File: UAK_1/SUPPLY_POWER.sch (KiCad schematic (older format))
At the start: 25 parts, among them X5 Крепежное_отверстие_d2, X6 Крепежное_отверстие_d2, X7 Крепежное_отверстие_d2

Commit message: 1B: заменены предохранители,обновлено питание,не добавлен второй дисплей
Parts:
- removed C11, C14: Конденсатор_керамический, N_RLC:Конденсатор_SMD_0603, symbol elements:Конденсатор_керамический
- removed DD2: Микросхема_DCDC_step_DOWN_MP2307DN, N_DD:SO-8_EP, symbol UAK_1-rescue:Микросхема_DCDC_step_DOWN_MP2307DN-elements_2020-UAK_0-rescue
- removed FU1: Предохранитель, N_RLC:Предохранитель_SMD_1812, symbol elements:Предохранитель
- removed G1: AC-DC-преобразователь_IRM-20-12, N_G:AC-DC_IRM-20-12, symbol UAK_1-rescue:AC-DC-преобразователь_IRM-20-12-elements_2020-UAK_0-rescue
- removed R18: Резистор_0,065Вт, N_RLC:Резистор_SMD_0603_0,065_Вт, symbol elements:Резистор_0,065Вт
- removed VD4, VD5: Диод_шоттки_SK16, N_VD_HL:Диод_SMB, symbol UAK_1-rescue:Диод_шоттки_SK16-elements_2020-UAK_0-rescue
- removed X5, X6, X7: Крепежное_отверстие_d2, MOTOR_ICO:Монтажное_отверстие_D2, symbol UAK_1-rescue:Крепежное_отверстие_d2-MOTOR_2020_components-UAK_0-rescue
- added DD2: Микросхема_DCDC_step_UP_LM2703, N_G:Преобразователь_LM2703_SOT-23-5, symbol elements:Микросхема_DCDC_step_UP_LM2703
- added G1: AC-DC-преобразователь_IRM-15-5, N_G:AC-DC_IRM-20-12, symbol elements_2020:AC-DC-преобразователь_IRM-15-5
- added VD2: Диод_шоттки_SK16, N_VD_HL:Диод_SMB, symbol UAK_1-rescue:Диод_шоттки_SK16-elements_2020-UAK_0-rescue
- C7: INFO 0,1мкФ/50В -> 10мкФ/25В; LINK https://www.chipdip.ru/product0/226236018 -> https://www.chipdip.ru/product/grm188r61e106m
- C8: INFO 10мкФ/25В -> 220пФ/50В; LINK https://www.chipdip.ru/product/grm188r61e106m -> https://www.chipdip.ru/product/grm188r71h392k
- C9: INFO 3900пФ/50В -> 10мкФ/25В; LINK https://www.chipdip.ru/product/grm188r71h392k -> https://www.chipdip.ru/product/grm188r61e106m
- L1: value Чип-индуктивность_10мкГн_1.8А_20проц. -> Чип-индуктивность_10мкГн_0.2А_20проц.; footprint N_RLC:Чип-индуктивность_SMD_SCD0503T -> N_RLC:Чип-индуктивность_SMD_0805; INFO 10мкГн/1,8А -> 10мкГн/0,2А; LINK https://www.chipdip.ru/product0/9000523874 -> https://www.chipdip.ru/product/mlz2012m100ht000-10
- R15: INFO 100 кОм -> 10 кОм
- R16: INFO 6,8 кОм -> 13,3 кОм
- R17: INFO 44,2 кОм -> 117 кОм
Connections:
- net labels added: 5V_NOISE
- net labels removed: 0V_RESERV, 12V_NOISE, 12V_OUT_G, 12V_RESERV, 5V_DC-DC, BOTTOM
- wire segments 85 -> 74
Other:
- note removed: "DC/DC 12V-5V + ОТВЕРСТИЯ ДЛЯ УСТАНОВКИ ПОКУПНОГО DC/DC НА СЛУЧАЙ НЕУДАЧИ"
- moved on the sheet: C10, C13, C16, L2

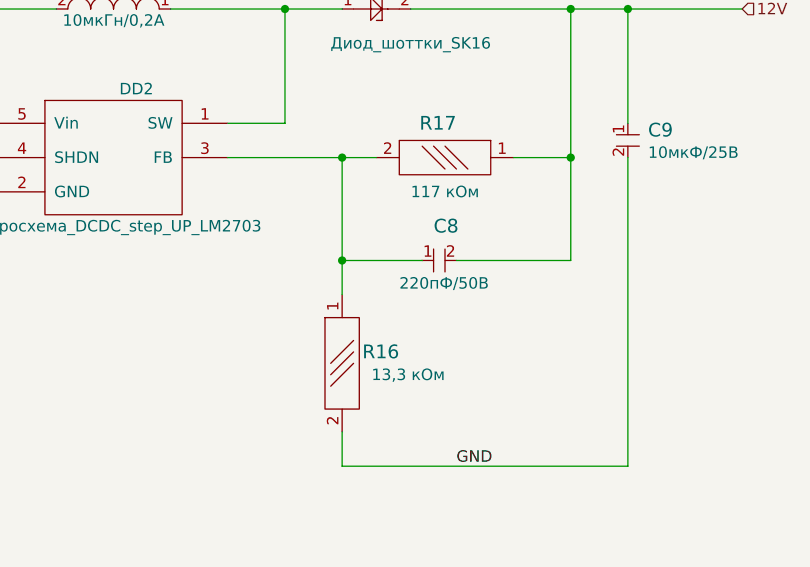
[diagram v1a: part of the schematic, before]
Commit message: обновлен перечень элементов
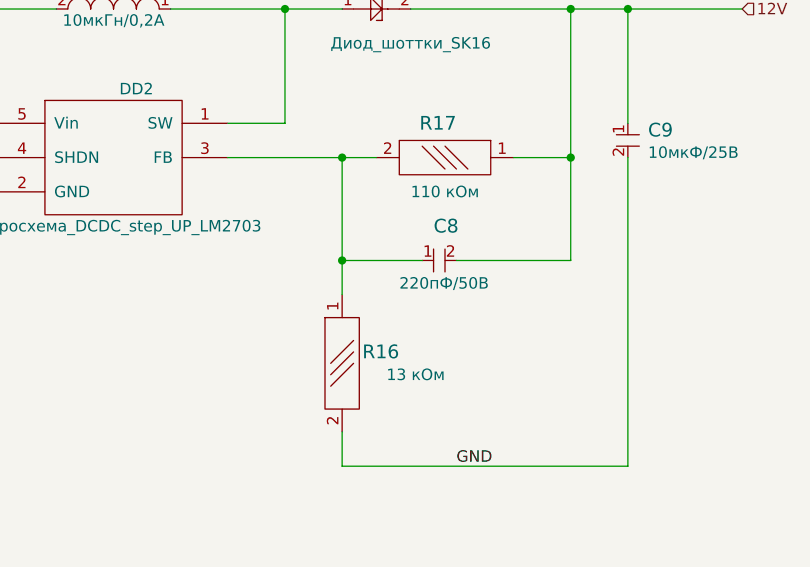
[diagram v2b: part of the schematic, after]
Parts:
- C10: Для заказа (none) -> Конденсатор 1210 0,022 мкФ 630В 10%
- C12, C13, C15, C16, C7, C9: LINK https://www.chipdip.ru/product/grm188r61e106m -> https://www.terraelectronica.ru/product/1489875; Для заказа (none) -> Конденсатор 0603 10 мкФ 25В 20%
- C8: LINK https://www.chipdip.ru/product/grm188r71h392k -> https://www.terraelectronica.ru/product/664080; Для заказа (none) -> Конденсатор 0603 220 пФ 50В 5%
- DD2: LINK (none) -> https://www.terraelectronica.ru/product/287900; Для заказа (none) -> DC-DC LM27313XMF/NOPB
- G1: Для заказа (none) -> AC-DC IRM-15-5
- G2: Для заказа (none) -> LDO LM1117GS-3.3
- L1: Для заказа (none) -> Чип-индуктивность 0805 10 мкГн 0,2А 20%
- L2: Для заказа (none) -> Дроссель B82731-T2132-A20
- R15: LINK (none) -> https://www.terraelectronica.ru/product/562124; Для заказа (none) -> Резистор 0603 10 кОм 5%
- R16: INFO 13,3 кОм -> 13 кОм; LINK (none) -> https://www.terraelectronica.ru/product/2782113; Для заказа (none) -> Резистор 0603 13 кОм 5%
- R17: INFO 117 кОм -> 110 кОм; Для заказа (none) -> Резистор 0603 110 кОм 5%
- VD2: LINK https://www.chipdip.ru/product/sk16-diotec -> https://www.terraelectronica.ru/product/129173; Для заказа (none) -> Диод шоттки SK16 (1А 60В)
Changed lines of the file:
@@
 F 4 "0,022мкФ/630В" V 3328 1788 50  0000 L CNN "INFO"
 F 5 "https://www.chipdip.ru/product/grm32qr72j223k" H 3250 1700 50  0001 C CNN "LINK"
+F 6 "Конденсатор 1210 0,022 мкФ 630В 10%" H 3250 1700 50  0001 C CNN "Для заказа"
 	1    3250 1700
 	0    1    1    0
@@
 F 3 "" H 6250 1650 60  0001 C CNN
 F 4 "10мкФ/25В" V 6328 1738 50  0000 L CNN "INFO"
-F 5 "https://www.chipdip.ru/product/grm188r61e106m" H 6250 1650 50  0001 C CNN "LINK"
+F 5 "https://www.terraelectronica.ru/product/1489875" H 6250 1650 50  0001 C CNN "LINK"
+F 6 "Конденсатор 0603 10 мкФ 25В 20%" H 6250 1650 50  0001 C CNN "Для заказа"
 	1    6250 1650
 	0    1    1    0
@@
 F 4 "https://www.chipdip.ru/product/b82731-t2132-a20" V 7250 1600 50  0001 C CNN "LINK"
 F 5 "2x6,8мГн/1,3А" V 7450 1650 50  0000 L CNN "INFO"
+F 6 "Дроссель B82731-T2132-A20" H 7250 1600 50  0001 C CNN "Для заказа"
 	1    7250 1600
 	0    1    1    0
@@
 F 3 "" H 8000 1650 60  0001 C CNN
 F 4 "10мкФ/25В" V 8078 1738 50  0000 L CNN "INFO"
-F 5 "https://www.chipdip.ru/product/grm188r61e106m" H 8000 1650 50  0001 C CNN "LINK"
+F 5 "https://www.terraelectronica.ru/product/1489875" H 8000 1650 50  0001 C CNN "LINK"
+F 6 "Конденсатор 0603 10 мкФ 25В 20%" H 8000 1650 50  0001 C CNN "Для заказа"
 	1    8000 1650
 	0    1    1    0
@@
 F 3 "https://static.chipdip.ru/lib/138/DOC004138838.pdf" H 4550 6000 50  0001 C CNN
 F 4 "https://www.chipdip.ru/product/lm1117gs-3.3" H 4550 6000 50  0001 C CNN "LINK"
+F 5 "LDO LM1117GS-3.3" H 4550 6000 50  0001 C CNN "Для заказа"
 	1    4550 6000
 	1    0    0    -1
@@
 F 3 "" H 4000 6150 60  0001 C CNN
 F 4 "10мкФ/25В" V 4078 6238 50  0000 L CNN "INFO"
-F 5 "https://www.chipdip.ru/product/grm188r61e106m" H 4000 6150 50  0001 C CNN "LINK"
+F 5 "https://www.terraelectronica.ru/product/1489875" H 4000 6150 50  0001 C CNN "LINK"
+F 6 "Конденсатор 0603 10 мкФ 25В 20%" H 4000 6150 50  0001 C CNN "Для заказа"
 	1    4000 6150
 	0    1    1    0
@@
 F 3 "" H 5500 6150 60  0001 C CNN
 F 4 "10мкФ/25В" V 5578 6238 50  0000 L CNN "INFO"
-F 5 "https://www.chipdip.ru/product/grm188r61e106m" H 5500 6150 50  0001 C CNN "LINK"
+F 5 "https://www.terraelectronica.ru/product/1489875" H 5500 6150 50  0001 C CNN "LINK"
+F 6 "Конденсатор 0603 10 мкФ 25В 20%" H 5500 6150 50  0001 C CNN "Для заказа"
 	1    5500 6150
 	0    1    1    0
@@
 F 4 "https://www.chipdip.ru/product/irm-15-5" H 4650 1100 50  0001 C CNN "LINK"
 F 5 "220В/5В" H 4650 1300 50  0000 C CNN "INFO"
+F 6 "AC-DC IRM-15-5" H 4300 1500 50  0001 C CNN "Для заказа"
 	1    4300 1500
 	1    0    0    -1
@@
 F 2 "N_G:Преобразователь_LM2703_SOT-23-5" H 5450 3500 50  0001 C CNN
 F 3 "" H 5450 3500 50  0001 C CNN
+F 4 "https://www.terraelectronica.ru/product/287900" H 5450 3500 50  0001 C CNN "LINK"
+F 5 "DC-DC LM27313XMF/NOPB" H 5450 3500 50  0001 C CNN "Для заказа"
 	1    5450 3500
 	1    0    0    -1
@@
 F 4 "10мкГн/0,2А" H 5350 2950 50  0000 C CNN "INFO"
 F 5 "https://www.chipdip.ru/product/mlz2012m100ht000-10" H 5400 2825 50  0001 C CNN "LINK"
+F 6 "Чип-индуктивность 0805 10 мкГн 0,2А 20%" H 5550 3000 50  0001 C CNN "Для заказа"
 	1    5550 3000
 	-1   0    0    -1
@@
 F 3 "https://static.chipdip.ru/lib/046/DOC003046730.pdf" H 6650 3000 50  0001 C CNN
 F 4 "1А, 60В" H 6925 2550 50  0001 C CNN "INFO"
-F 5 "https://www.chipdip.ru/product/sk16-diotec" H 6925 2675 50  0001 C CNN "LINK"
+F 5 "https://www.terraelectronica.ru/product/129173" H 6925 2675 50  0001 C CNN "LINK"
+F 6 "Диод шоттки SK16 (1А 60В)" H 6750 3000 50  0001 C CNN "Для заказа"
 	1    6750 3000
 	1    0    0    -1
@@
 F 3 "" H 4000 3550 60  0001 C CNN
 F 4 "10мкФ/25В" V 4078 3638 50  0000 L CNN "INFO"
-F 5 "https://www.chipdip.ru/product/grm188r61e106m" H 4000 3550 50  0001 C CNN "LINK"
+F 5 "https://www.terraelectronica.ru/product/1489875" H 4000 3550 50  0001 C CNN "LINK"
+F 6 "Конденсатор 0603 10 мкФ 25В 20%" H 4000 3550 50  0001 C CNN "Для заказа"
 	1    4000 3550
 	0    -1   1    0
@@
 F 3 "" H 8000 3550 60  0001 C CNN
 F 4 "10мкФ/25В" V 8078 3638 50  0000 L CNN "INFO"
-F 5 "https://www.chipdip.ru/product/grm188r61e106m" H 8000 3550 50  0001 C CNN "LINK"
+F 5 "https://www.terraelectronica.ru/product/1489875" H 8000 3550 50  0001 C CNN "LINK"
+F 6 "Конденсатор 0603 10 мкФ 25В 20%" H 8000 3550 50  0001 C CNN "Для заказа"
 	1    8000 3550
 	0    1    1    0
@@
 F 2 "N_RLC:Резистор_SMD_0603_0,065_Вт" H 7200 3650 60  0001 C CNN
 F 3 "" H 7200 3650 60  0001 C CNN
-F 4 "117 кОм" H 7050 3500 50  0000 L CNN "INFO"
+F 4 "110 кОм" H 7050 3500 50  0000 L CNN "INFO"
+F 5 "Резистор 0603 110 кОм 5%" H 7200 3650 50  0001 C CNN "Для заказа"
 	1    7200 3650
 	-1   0    0    -1
@@
 F 2 "N_RLC:Резистор_SMD_0603_0,065_Вт" H 6750 4550 60  0001 C CNN
 F 3 "" H 6750 4550 60  0001 C CNN
-F 4 "13,3 кОм" V 6800 4100 50  0000 L CNN "INFO"
+F 4 "13 кОм" V 6800 4100 50  0000 L CNN "INFO"
+F 5 "Резистор 0603 13 кОм 5%" H 6750 4550 50  0001 C CNN "Для заказа"
+F 6 "https://www.terraelectronica.ru/product/2782113" H 6750 4550 50  0001 C CNN "LINK"
 	1    6750 4550
 	0    -1   1    0
@@
 F 3 "" H 7150 4100 60  0001 C CNN
 F 4 "220пФ/50В" H 7000 4000 50  0000 L CNN "INFO"
-F 5 "https://www.chipdip.ru/product/grm188r71h392k" H 7150 4100 50  0001 C CNN "LINK"
+F 5 "https://www.terraelectronica.ru/product/664080" H 7150 4100 50  0001 C CNN "LINK"
+F 6 "Конденсатор 0603 220 пФ 50В 5%" H 7150 4100 50  0001 C CNN "Для заказа"
 	1    7150 4100
 	1    0    0    -1
@@
 F 3 "" H 4250 3550 60  0001 C CNN
 F 4 "10 кОм" V 4300 3150 50  0000 L CNN "INFO"
+F 5 "https://www.terraelectronica.ru/product/562124" H 4250 3550 50  0001 C CNN "LINK"
+F 6 "Резистор 0603 10 кОм 5%" H 4250 3550 50  0001 C CNN "Для заказа"
 	1    4250 3550
 	0    -1   1    0

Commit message: UAK.1C.M9, подготовлены gerber, схема, BOM
обновлена маркировка, заполнен BOM
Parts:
- G1: symbol elements_2020:AC-DC-преобразователь_IRM-15-5 -> UAK_1-rescue:AC-DC-преобразователь_IRM-15-5-elements_2020
- R16: INFO 13 кОм -> 10 кОм; LINK https://www.terraelectronica.ru/product/2782113 -> https://www.terraelectronica.ru/product/562124; Для заказа Резистор 0603 13 кОм 5% -> Резистор 0603 10 кОм 5%
- R17: INFO 110 кОм -> 82 кОм; LINK (none) -> https://www.terraelectronica.ru/product/2782214; Для заказа Резистор 0603 110 кОм 5% -> Резистор 0603 82 кОм 5%
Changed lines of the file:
@@
 EESchema Schematic File Version 4
 LIBS:UAK_1-cache
-EELAYER 30 0
+EELAYER 29 0
 EELAYER END
 $Descr A4 11693 8268
@@
 5V_NOISE
 $Comp
-L elements_2020:AC-DC-преобразователь_IRM-15-5 G1
+L UAK_1-rescue:AC-DC-преобразователь_IRM-15-5-elements_2020 G1
 U 1 1 5F6F4DEB
 P 4300 1500
+AR Path="/5F6F4DEB" Ref="G1"  Part="1"
+AR Path="/5F540B17/5F6F4DEB" Ref="G1"  Part="1"
 F 0 "G1" H 4850 1600 50  0000 C CNN
 F 1 "AC-DC-преобразователь_IRM-15-5" H 4650 1724 50  0001 C CNN
@@
 F 2 "N_RLC:Резистор_SMD_0603_0,065_Вт" H 7200 3650 60  0001 C CNN
 F 3 "" H 7200 3650 60  0001 C CNN
-F 4 "110 кОм" H 7050 3500 50  0000 L CNN "INFO"
-F 5 "Резистор 0603 110 кОм 5%" H 7200 3650 50  0001 C CNN "Для заказа"
+F 4 "82 кОм" H 7050 3500 50  0000 L CNN "INFO"
+F 5 "Резистор 0603 82 кОм 5%" H 7200 3650 50  0001 C CNN "Для заказа"
+F 6 "https://www.terraelectronica.ru/product/2782214" H 7200 3650 50  0001 C CNN "LINK"
 	1    7200 3650
 	-1   0    0    -1
@@
 F 2 "N_RLC:Резистор_SMD_0603_0,065_Вт" H 6750 4550 60  0001 C CNN
 F 3 "" H 6750 4550 60  0001 C CNN
-F 4 "13 кОм" V 6800 4100 50  0000 L CNN "INFO"
-F 5 "Резистор 0603 13 кОм 5%" H 6750 4550 50  0001 C CNN "Для заказа"
-F 6 "https://www.terraelectronica.ru/product/2782113" H 6750 4550 50  0001 C CNN "LINK"
+F 4 "10 кОм" V 6800 4100 50  0000 L CNN "INFO"
+F 5 "Резистор 0603 10 кОм 5%" H 6750 4550 50  0001 C CNN "Для заказа"
+F 6 "https://www.terraelectronica.ru/product/562124" H 6750 4550 50  0001 C CNN "LINK"
 	1    6750 4550
 	0    -1   1    0
